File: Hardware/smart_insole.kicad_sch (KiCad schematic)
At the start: 16 parts, among them Y2 32MHz

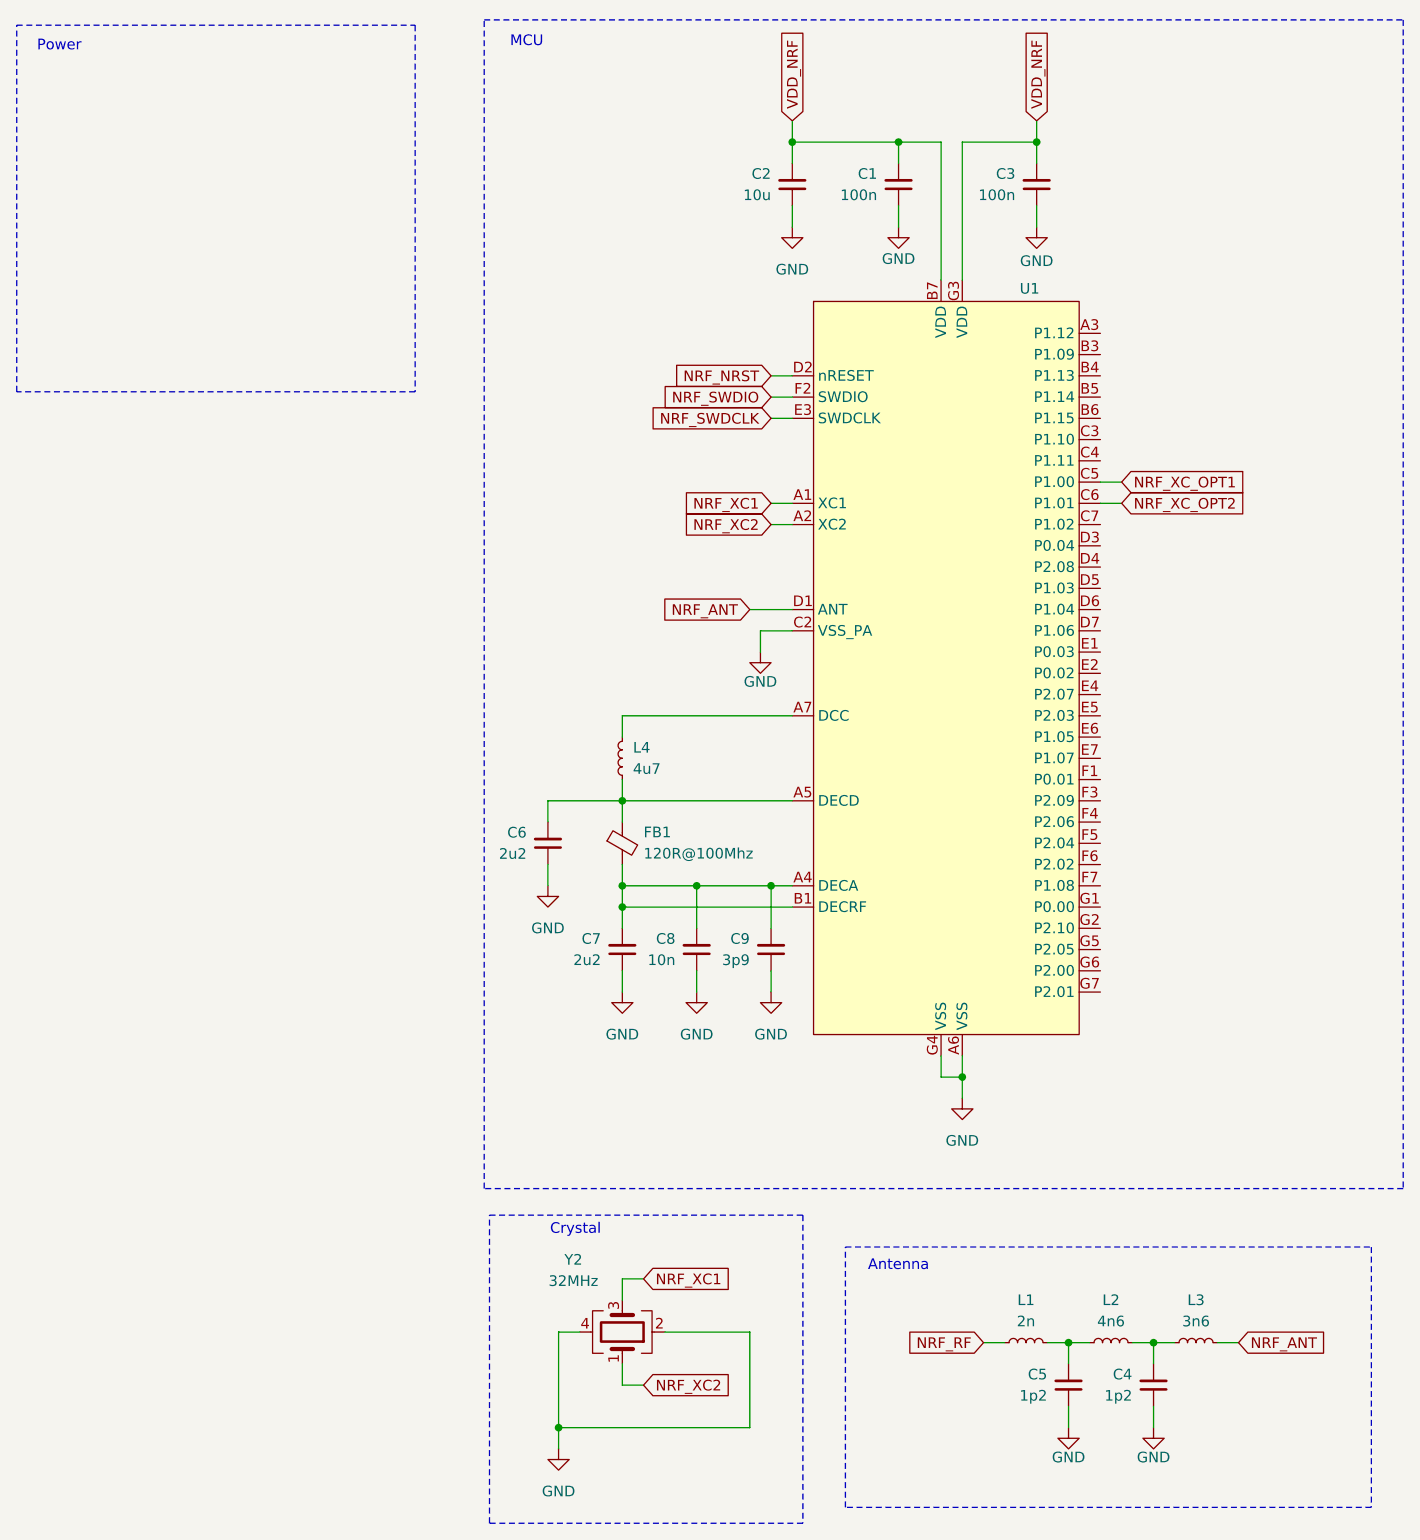
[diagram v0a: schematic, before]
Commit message: added MFN to nRF54L15-CAAA
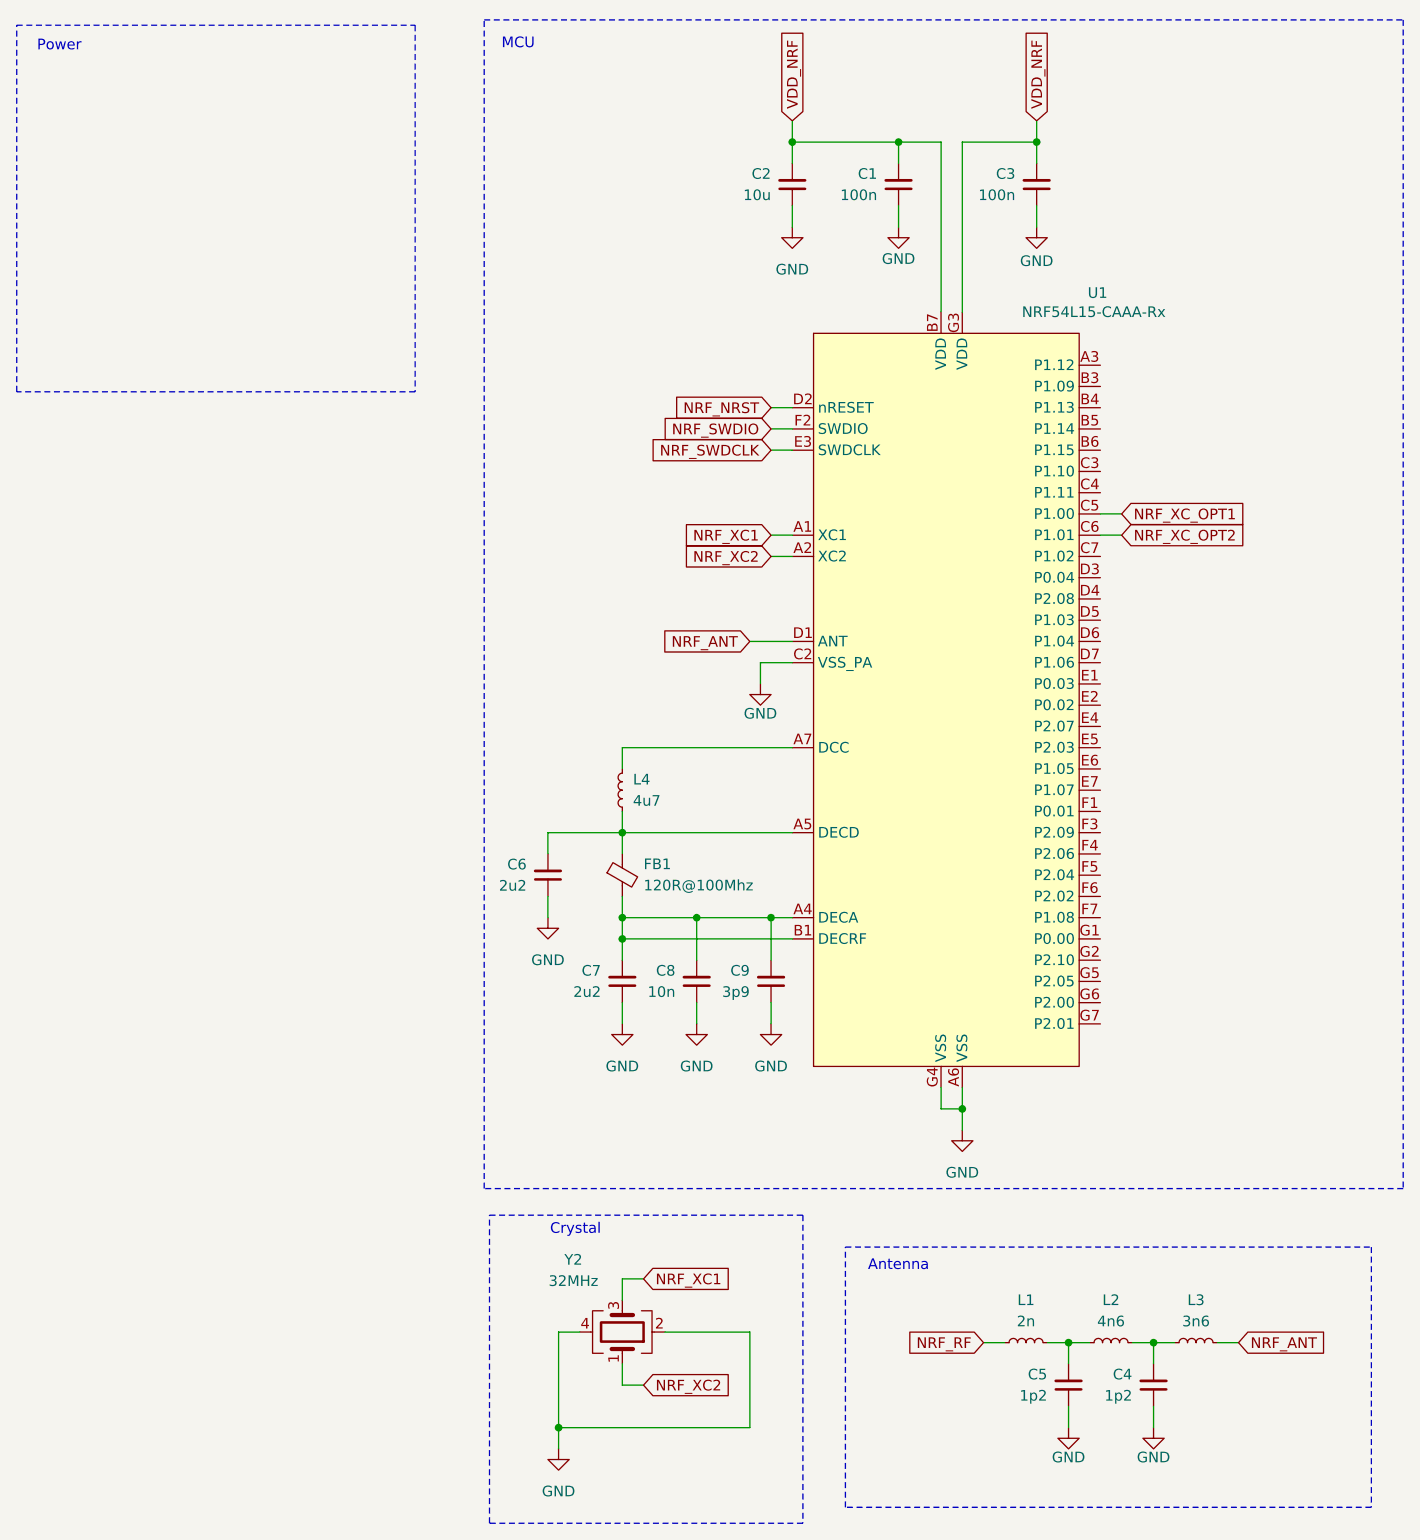
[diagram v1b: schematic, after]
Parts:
- U1: value ~ -> NRF54L15-CAAA-Rx; MFN (none) -> NRF54L15-CAAA-R
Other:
- moved on the sheet: C6, C7, C8, C9, FB1, L4, U1
